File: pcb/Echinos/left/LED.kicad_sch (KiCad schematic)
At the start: 14 parts

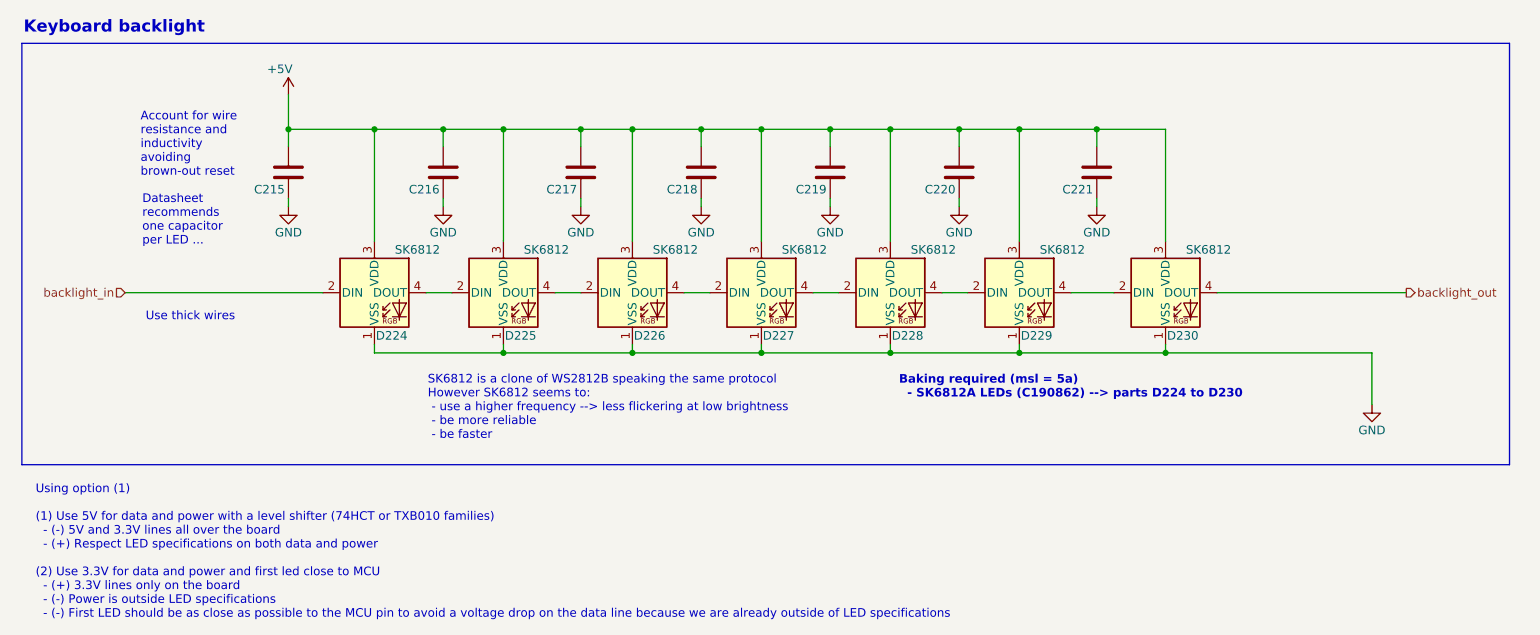
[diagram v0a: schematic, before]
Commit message: 💥 [PCB] - Split schematic for left and right halves.   - Required to create a common PCB to lower the manufacturing cost
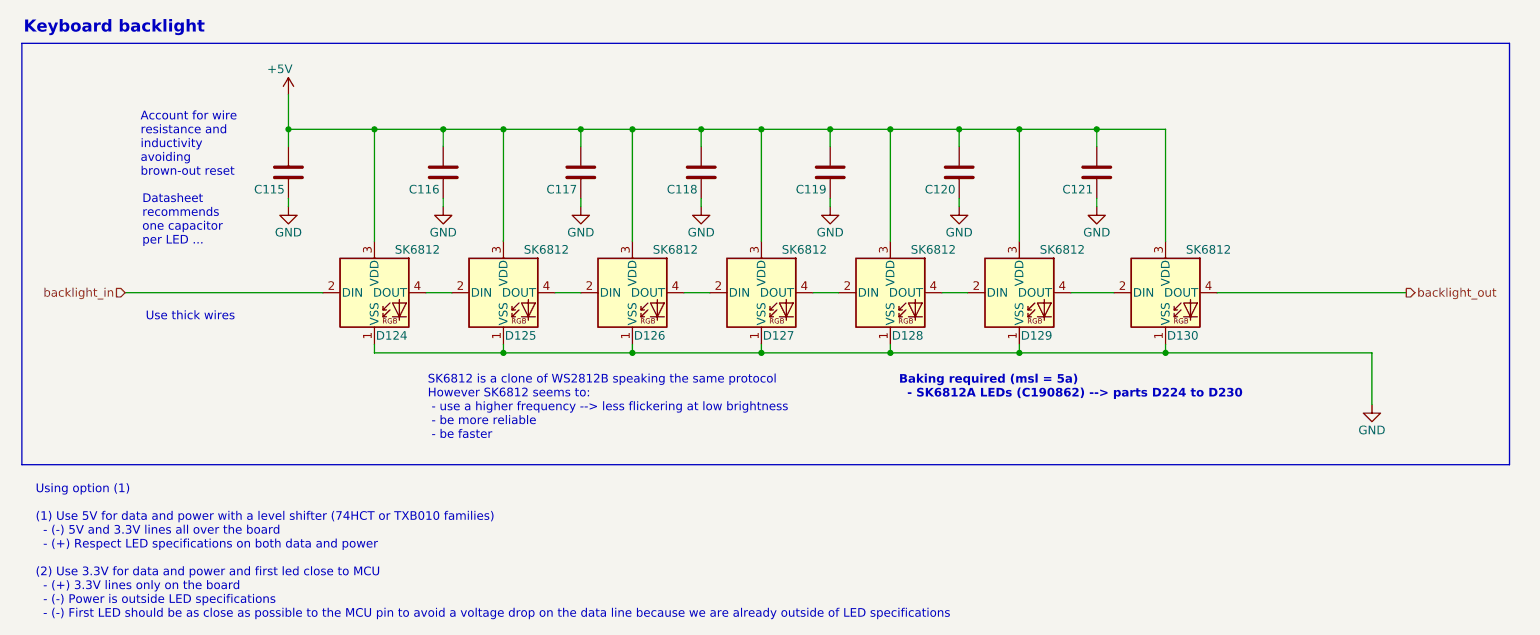
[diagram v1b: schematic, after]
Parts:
- renumbered C215 to C115, C216 to C116, C217 to C117, C218 to C118, C219 to C119, C220 to C120, C221 to C121, D224 to D124, D225 to D125, D226 to D126, D227 to D127, D228 to D128, D229 to D129, D230 to D130
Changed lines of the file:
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@@
 		(in_pos_files yes)
 		(dnp no)
-		(property "Reference" "D227"
+		(property "Reference" "D127"
 			(at 130.81 61.595 0)
 			(show_name no)
@@
 			(project "Echinos_Left"
 				(path "/5bd3006d-ec09-4ffb-bec3-03fa5613b46a/543aedce-e9ee-4fb5-8ab9-5c11613569bb/d7b817c5-5130-4c2e-ac26-b341cad9c61d"
-					(reference "D227")
+					(reference "D127")
 					(unit 1)
 				)
@@
 		(in_pos_files yes)
 		(dnp no)
-		(property "Reference" "D224"
+		(property "Reference" "D124"
 			(at 73.66 61.595 0)
 			(show_name no)
@@
 			(project "Echinos_Left"
 				(path "/5bd3006d-ec09-4ffb-bec3-03fa5613b46a/543aedce-e9ee-4fb5-8ab9-5c11613569bb/d7b817c5-5130-4c2e-ac26-b341cad9c61d"
-					(reference "D224")
+					(reference "D124")
 					(unit 1)
 				)
@@
 		(in_pos_files yes)
 		(dnp no)
-		(property "Reference" "C220"
+		(property "Reference" "C120"
 			(at 152.4 40.005 0)
 			(show_name no)
@@
 			(project "Echinos_Left"
 				(path "/5bd3006d-ec09-4ffb-bec3-03fa5613b46a/543aedce-e9ee-4fb5-8ab9-5c11613569bb/d7b817c5-5130-4c2e-ac26-b341cad9c61d"
-					(reference "C220")
+					(reference "C120")
 					(unit 1)
 				)
@@
 		(in_pos_files yes)
 		(dnp no)
-		(property "Reference" "C221"
+		(property "Reference" "C121"
 			(at 172.72 40.005 0)
 			(show_name no)
@@
 			(project "Echinos_Left"
 				(path "/5bd3006d-ec09-4ffb-bec3-03fa5613b46a/543aedce-e9ee-4fb5-8ab9-5c11613569bb/d7b817c5-5130-4c2e-ac26-b341cad9c61d"
-					(reference "C221")
+					(reference "C121")
 					(unit 1)
 				)
@@
 		(in_pos_files yes)
 		(dnp no)
-		(property "Reference" "C217"
+		(property "Reference" "C117"
 			(at 96.52 40.005 0)
 			(show_name no)
@@
 			(project "Echinos_Left"
 				(path "/5bd3006d-ec09-4ffb-bec3-03fa5613b46a/543aedce-e9ee-4fb5-8ab9-5c11613569bb/d7b817c5-5130-4c2e-ac26-b341cad9c61d"
-					(reference "C217")
+					(reference "C117")
 					(unit 1)
 				)
@@
 		(in_pos_files yes)
 		(dnp no)
-		(property "Reference" "#PWR0220"
+		(property "Reference" "#PWR0120"
 			(at 177.8 48.895 0)
 			(hide yes)
@@
 			(project "Echinos_Left"
 				(path "/5bd3006d-ec09-4ffb-bec3-03fa5613b46a/543aedce-e9ee-4fb5-8ab9-5c11613569bb/d7b817c5-5130-4c2e-ac26-b341cad9c61d"
-					(reference "#PWR0220")
+					(reference "#PWR0120")
 					(unit 1)
 				)
@@
 		(in_pos_files yes)
 		(dnp no)
-		(property "Reference" "#PWR0215"
+		(property "Reference" "#PWR0115"
 			(at 81.28 48.895 0)
 			(hide yes)
@@
 			(project "Echinos_Left"
 				(path "/5bd3006d-ec09-4ffb-bec3-03fa5613b46a/543aedce-e9ee-4fb5-8ab9-5c11613569bb/d7b817c5-5130-4c2e-ac26-b341cad9c61d"
-					(reference "#PWR0215")
+					(reference "#PWR0115")
 					(unit 1)
 				)
@@
 		(in_pos_files yes)
 		(dnp no)
-		(property "Reference" "D230"
+		(property "Reference" "D130"
 			(at 190.5 61.595 0)
 			(show_name no)
@@
 			(project "Echinos_Left"
 				(path "/5bd3006d-ec09-4ffb-bec3-03fa5613b46a/543aedce-e9ee-4fb5-8ab9-5c11613569bb/d7b817c5-5130-4c2e-ac26-b341cad9c61d"
-					(reference "D230")
+					(reference "D130")
 					(unit 1)
 				)
@@
 		(in_pos_files yes)
 		(dnp no)
-		(property "Reference" "#PWR0213"
+		(property "Reference" "#PWR0113"
 			(at 58.42 29.845 0)
 			(hide yes)
@@
 			(project "Echinos_Left"
 				(path "/5bd3006d-ec09-4ffb-bec3-03fa5613b46a/543aedce-e9ee-4fb5-8ab9-5c11613569bb/d7b817c5-5130-4c2e-ac26-b341cad9c61d"
-					(reference "#PWR0213")
+					(reference "#PWR0113")
 					(unit 1)
 				)
@@
 		(in_pos_files yes)
 		(dnp no)
-		(property "Reference" "#PWR0221"
+		(property "Reference" "#PWR0121"
 			(at 218.44 78.105 0)
 			(hide yes)
@@
 			(project "Echinos_Left"
 				(path "/5bd3006d-ec09-4ffb-bec3-03fa5613b46a/543aedce-e9ee-4fb5-8ab9-5c11613569bb/d7b817c5-5130-4c2e-ac26-b341cad9c61d"
-					(reference "#PWR0221")
+					(reference "#PWR0121")
 					(unit 1)
 				)
@@
 		(in_pos_files yes)
 		(dnp no)
-		(property "Reference" "C215"
+		(property "Reference" "C115"
 			(at 53.34 40.005 0)
 			(show_name no)
@@
 			(project "Echinos_Left"
 				(path "/5bd3006d-ec09-4ffb-bec3-03fa5613b46a/543aedce-e9ee-4fb5-8ab9-5c11613569bb/d7b817c5-5130-4c2e-ac26-b341cad9c61d"
-					(reference "C215")
+					(reference "C115")
 					(unit 1)
 				)
@@
 		(in_pos_files yes)
 		(dnp no)
-		(property "Reference" "C216"
+		(property "Reference" "C116"
 			(at 76.2 40.005 0)
 			(show_name no)
@@
 			(project "Echinos_Left"
 				(path "/5bd3006d-ec09-4ffb-bec3-03fa5613b46a/543aedce-e9ee-4fb5-8ab9-5c11613569bb/d7b817c5-5130-4c2e-ac26-b341cad9c61d"
-					(reference "C216")
+					(reference "C116")
 					(unit 1)
 				)
@@
 		(in_pos_files yes)
 		(dnp no)
-		(property "Reference" "C219"
+		(property "Reference" "C119"
 			(at 133.35 40.005 0)
 			(show_name no)
@@
 			(project "Echinos_Left"
 				(path "/5bd3006d-ec09-4ffb-bec3-03fa5613b46a/543aedce-e9ee-4fb5-8ab9-5c11613569bb/d7b817c5-5130-4c2e-ac26-b341cad9c61d"
-					(reference "C219")
+					(reference "C119")
 					(unit 1)
 				)
@@
 		(in_pos_files yes)
 		(dnp no)
-		(property "Reference" "C218"
+		(property "Reference" "C118"
 			(at 114.3 40.005 0)
 			(show_name no)
@@
 			(project "Echinos_Left"
 				(path "/5bd3006d-ec09-4ffb-bec3-03fa5613b46a/543aedce-e9ee-4fb5-8ab9-5c11613569bb/d7b817c5-5130-4c2e-ac26-b341cad9c61d"
-					(reference "C218")
+					(reference "C118")
 					(unit 1)
 				)
@@
 		(in_pos_files yes)
 		(dnp no)
-		(property "Reference" "D228"
+		(property "Reference" "D128"
 			(at 149.86 61.595 0)
 			(show_name no)
@@
 			(project "Echinos_Left"
 				(path "/5bd3006d-ec09-4ffb-bec3-03fa5613b46a/543aedce-e9ee-4fb5-8ab9-5c11613569bb/d7b817c5-5130-4c2e-ac26-b341cad9c61d"
-					(reference "D228")
+					(reference "D128")
 					(unit 1)
 				)
@@
 		(in_pos_files yes)
 		(dnp no)
-		(property "Reference" "#PWR0219"
+		(property "Reference" "#PWR0119"
 			(at 157.48 48.895 0)
 			(hide yes)
@@
 			(project "Echinos_Left"
 				(path "/5bd3006d-ec09-4ffb-bec3-03fa5613b46a/543aedce-e9ee-4fb5-8ab9-5c11613569bb/d7b817c5-5130-4c2e-ac26-b341cad9c61d"
-					(reference "#PWR0219")
+					(reference "#PWR0119")
 					(unit 1)
 				)
@@
 		(in_pos_files yes)
 		(dnp no)
-		(property "Reference" "#PWR0216"
+		(property "Reference" "#PWR0116"
 			(at 101.6 48.895 0)
 			(hide yes)
@@
 			(project "Echinos_Left"
 				(path "/5bd3006d-ec09-4ffb-bec3-03fa5613b46a/543aedce-e9ee-4fb5-8ab9-5c11613569bb/d7b817c5-5130-4c2e-ac26-b341cad9c61d"
-					(reference "#PWR0216")
+					(reference "#PWR0116")
 					(unit 1)
 				)
@@
 		(in_pos_files yes)
 		(dnp no)
-		(property "Reference" "D225"
+		(property "Reference" "D125"
 			(at 92.71 61.595 0)
 			(show_name no)
@@
 			(project "Echinos_Left"
 				(path "/5bd3006d-ec09-4ffb-bec3-03fa5613b46a/543aedce-e9ee-4fb5-8ab9-5c11613569bb/d7b817c5-5130-4c2e-ac26-b341cad9c61d"
-					(reference "D225")
+					(reference "D125")
 					(unit 1)
 				)
@@
 		(in_pos_files yes)
 		(dnp no)
-		(property "Reference" "#PWR0217"
+		(property "Reference" "#PWR0117"
 			(at 119.38 48.895 0)
 			(hide yes)
@@
 			(project "Echinos_Left"
 				(path "/5bd3006d-ec09-4ffb-bec3-03fa5613b46a/543aedce-e9ee-4fb5-8ab9-5c11613569bb/d7b817c5-5130-4c2e-ac26-b341cad9c61d"
-					(reference "#PWR0217")
+					(reference "#PWR0117")
 					(unit 1)
 				)
@@
 		(in_pos_files yes)
 		(dnp no)
-		(property "Reference" "#PWR0214"
+		(property "Reference" "#PWR0114"
 			(at 58.42 48.895 0)
 			(hide yes)
@@
 			(project "Echinos_Left"
 				(path "/5bd3006d-ec09-4ffb-bec3-03fa5613b46a/543aedce-e9ee-4fb5-8ab9-5c11613569bb/d7b817c5-5130-4c2e-ac26-b341cad9c61d"
-					(reference "#PWR0214")
+					(reference "#PWR0114")
 					(unit 1)
 				)
@@
 		(in_pos_files yes)
 		(dnp no)
-		(property "Reference" "D226"
+		(property "Reference" "D126"
 			(at 111.76 61.595 0)
 			(show_name no)
@@
 			(project "Echinos_Left"
 				(path "/5bd3006d-ec09-4ffb-bec3-03fa5613b46a/543aedce-e9ee-4fb5-8ab9-5c11613569bb/d7b817c5-5130-4c2e-ac26-b341cad9c61d"
-					(reference "D226")
+					(reference "D126")
 					(unit 1)
 				)
@@
 		(in_pos_files yes)
 		(dnp no)
-		(property "Reference" "D229"
+		(property "Reference" "D129"
 			(at 168.91 61.595 0)
 			(show_name no)
@@
 			(project "Echinos_Left"
 				(path "/5bd3006d-ec09-4ffb-bec3-03fa5613b46a/543aedce-e9ee-4fb5-8ab9-5c11613569bb/d7b817c5-5130-4c2e-ac26-b341cad9c61d"
-					(reference "D229")
+					(reference "D129")
 					(unit 1)
 				)
@@
 		(in_pos_files yes)
 		(dnp no)
-		(property "Reference" "#PWR0218"
+		(property "Reference" "#PWR0118"
 			(at 138.43 48.895 0)
 			(hide yes)
@@
 			(project "Echinos_Left"
 				(path "/5bd3006d-ec09-4ffb-bec3-03fa5613b46a/543aedce-e9ee-4fb5-8ab9-5c11613569bb/d7b817c5-5130-4c2e-ac26-b341cad9c61d"
-					(reference "#PWR0218")
+					(reference "#PWR0118")
 					(unit 1)
 				)
